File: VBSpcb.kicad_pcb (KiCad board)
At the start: 2 copper layers, 38 x 31.5 mm, 14 parts, among them J1 Conn_01x03, J2 DB25_Receptacle, U1 LF356

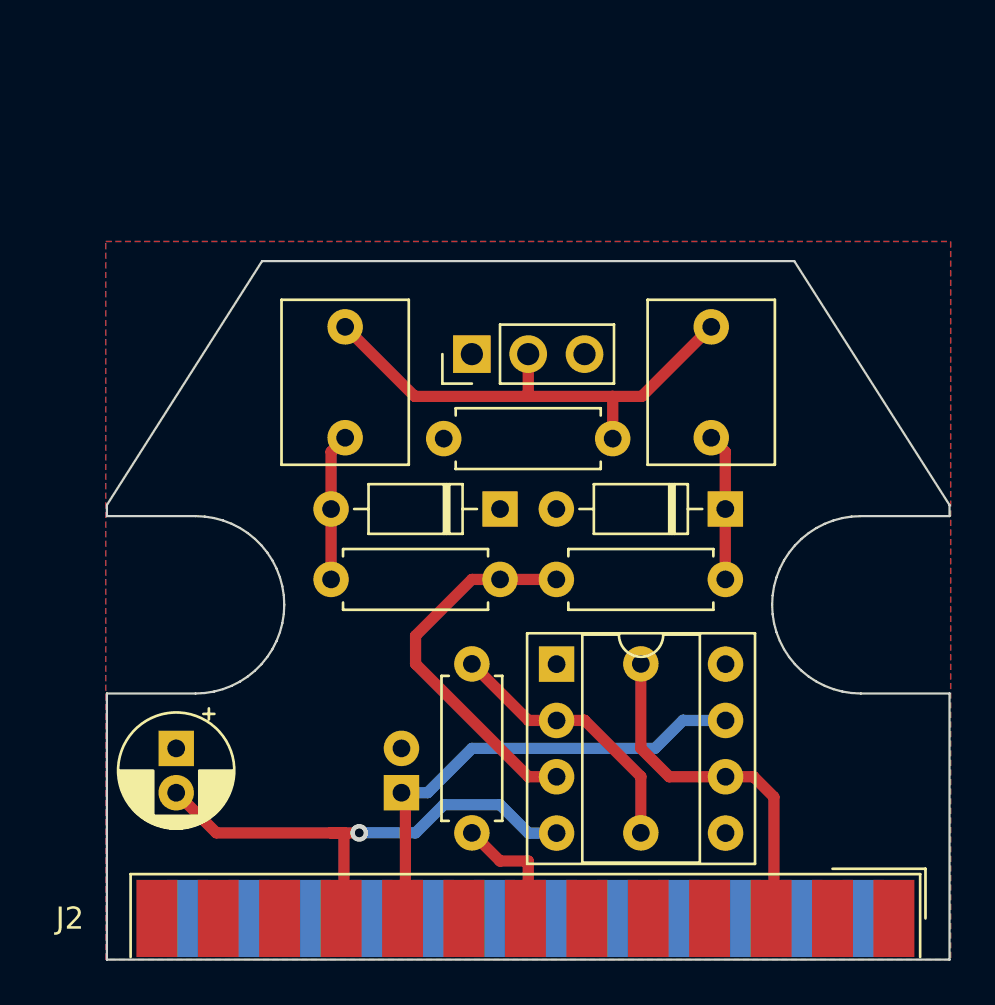
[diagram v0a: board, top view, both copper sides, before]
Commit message: Updated Silkscreen
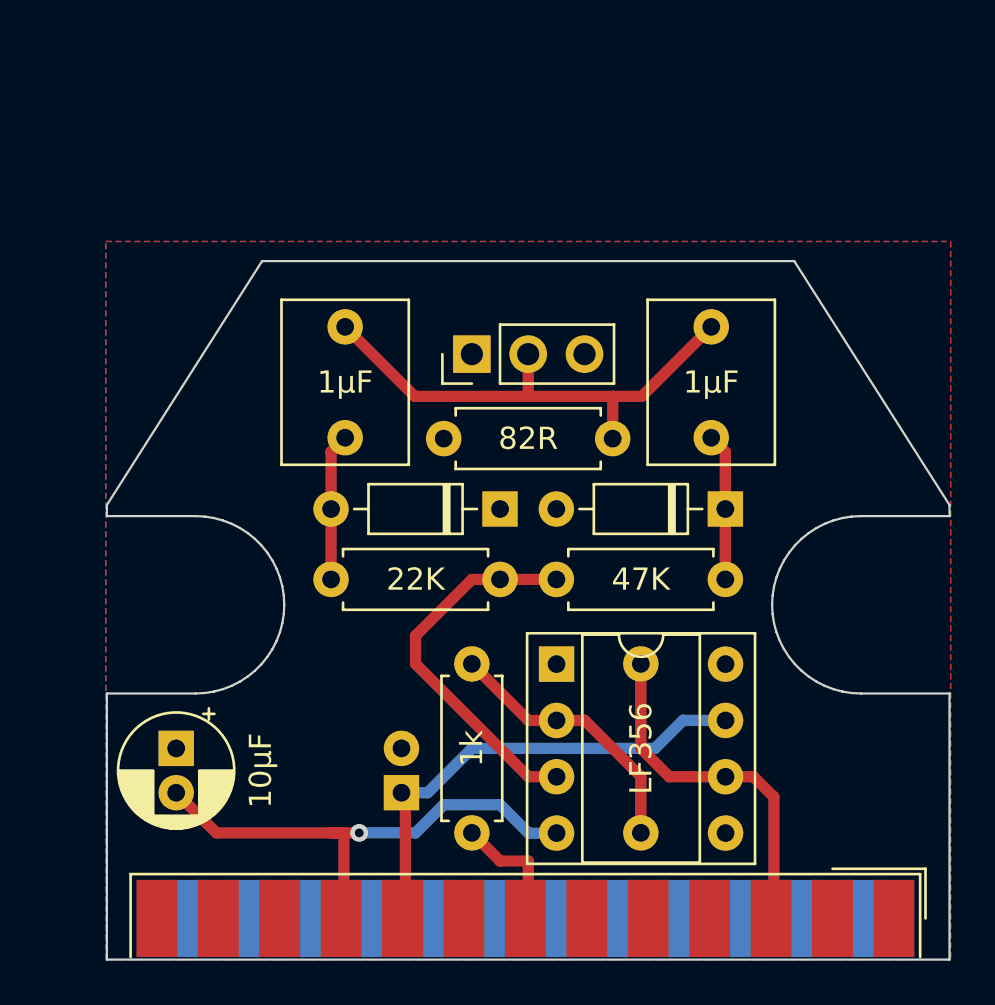
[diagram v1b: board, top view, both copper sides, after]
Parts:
- J1: value Conn_01x03 -> Video In
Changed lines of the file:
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@@
         (effects (font (size 1 1) (thickness 0.15)))
     )
-    (fp_text value "1µF" (at 2.5 0) (layer "F.Fab")
+    (fp_text value "1µF" (at 2.5 0) (layer "F.SilkS")
         (effects (font (size 1 1) (thickness 0.15)))
     )
@@
     (property "ki_keywords" "female receptacle D-SUB connector")
     (attr smd)
-    (fp_text reference "J2" (at -20.543333 0) (layer "F.SilkS")
-        (effects (font (size 1 1) (thickness 0.15)))
-    )
-    (fp_text value "DB25_Receptacle" (at 0 16.86) (layer "F.Fab")
-        (effects (font (size 1 1) (thickness 0.15)))
-    )
-    (fp_text user "PCB edge" (at -21.55 1.323333) (layer "Dwgs.User")
+    (fp_text reference "J2" (at -20.543333 0) (layer "F.SilkS") hide
+        (effects (font (size 1 1) (thickness 0.15)))
+    )
+    (fp_text value "DB25_Receptacle" (at 0 16.86) (layer "F.SilkS") hide
+        (effects (font (size 1 1) (thickness 0.15)))
+    )
+    (fp_text user "PCB edge" (at -21.55 1.323333) (layer "Dwgs.User") hide
         (effects (font (size 0.5 0.5) (thickness 0.075)))
     )
-    (fp_text user "${REFERENCE}" (at 0 3.39) (layer "F.Fab")
+    (fp_text user "${REFERENCE}" (at 0 3.39) (layer "F.Fab") hide
         (effects (font (size 1 1) (thickness 0.15)))
     )
@@
         (effects (font (size 1 1) (thickness 0.15)))
     )
-    (fp_text value "1N4148" (at 3.81 2.12) (layer "F.Fab") hide
+    (fp_text value "1N4148" (at 3.81 2.12) (layer "F.SilkS") hide
         (effects (font (size 1 1) (thickness 0.15)))
     )
@@
         (effects (font (size 1 1) (thickness 0.15)))
     )
-    (fp_text value "1k" (at 3.81 0 -270) (layer "F.Fab")
+    (fp_text value "1k" (at 3.81 0 -270) (layer "F.SilkS")
         (effects (font (size 1 1) (thickness 0.15)))
     )
@@
         (effects (font (size 1 1) (thickness 0.15)))
     )
-    (fp_text value "10µF" (at 1 -3.81 -270) (layer "F.Fab")
+    (fp_text value "10µF" (at 1 -3.81 -270) (layer "F.SilkS")
         (effects (font (size 1 1) (thickness 0.15)))
     )
@@
         (effects (font (size 1 1) (thickness 0.15)))
     )
-    (fp_text value "47K" (at 3.81 0) (layer "F.Fab")
+    (fp_text value "47K" (at 3.81 0) (layer "F.SilkS")
         (effects (font (size 1 1) (thickness 0.15)))
     )
@@
         (effects (font (size 1 1) (thickness 0.15)))
     )
-    (fp_text value "1N4148" (at 3.81 2.12) (layer "F.Fab") hide
+    (fp_text value "1N4148" (at 3.81 2.12) (layer "F.SilkS") hide
         (effects (font (size 1 1) (thickness 0.15)))
     )
@@
         (effects (font (size 1 1) (thickness 0.15)))
     )
-    (fp_text value "22K" (at 3.81 0) (layer "F.Fab")
+    (fp_text value "22K" (at 3.81 0) (layer "F.SilkS")
         (effects (font (size 1 1) (thickness 0.15)))
     )
@@
         (effects (font (size 1 1) (thickness 0.15)))
     )
-    (fp_text value "1µF" (at 2.5 0) (layer "F.Fab")
+    (fp_text value "1µF" (at 2.5 0) (layer "F.SilkS")
         (effects (font (size 1 1) (thickness 0.15)))
     )
@@
         (effects (font (size 1 1) (thickness 0.15)))
     )
-    (fp_text value "82R" (at 3.81 0) (layer "F.Fab")
+    (fp_text value "82R" (at 3.81 0) (layer "F.SilkS")
         (effects (font (size 1 1) (thickness 0.15)))
     )
@@
         (effects (font (size 1 1) (thickness 0.15)))
     )
-    (fp_text value "LF356" (at 3.81 3.8 90) (layer "F.Fab")
+    (fp_text value "LF356" (at 3.81 3.8 90) (layer "F.SilkS")
         (effects (font (size 1 1) (thickness 0.15)))
     )
@@
         (effects (font (size 1 1) (thickness 0.15)))
     )
-    (fp_text value "Conn_01x03" (at 0 7.41 90) (layer "F.Fab") hide
+    (fp_text value "Video In" (at 0 7.41 90) (layer "F.SilkS") hide
         (effects (font (size 1 1) (thickness 0.15)))
     )
@@
         (effects (font (size 1 1) (thickness 0.15)) (justify mirror))
     )
-    (fp_text value "9k1" (at 3.81 0 90) (layer "B.Fab")
+    (fp_text value "9k1" (at 3.81 0 90) (layer "B.SilkS")
         (effects (font (size 1 1) (thickness 0.15)) (justify mirror))
     )
@@
         (effects (font (size 1 1) (thickness 0.15)) (justify mirror))
     )
-    (fp_text value "10µF" (at 1 -3.75 90) (layer "B.Fab")
+    (fp_text value "10µF" (at 1 -3.75 90) (layer "B.SilkS")
         (effects (font (size 1 1) (thickness 0.15)) (justify mirror))
     )

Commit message: Added nubbin for strain releif
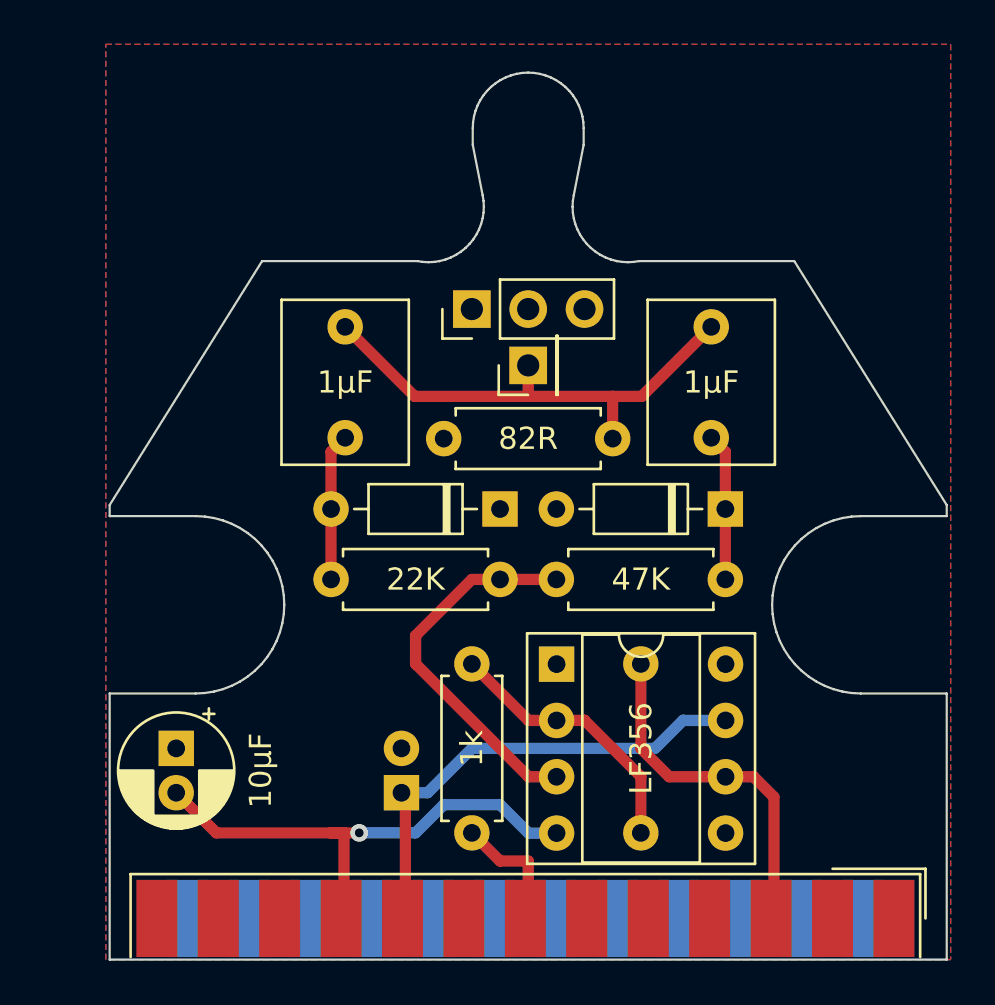
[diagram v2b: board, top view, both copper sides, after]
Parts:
- added J3: Video In Sig, Connector_PinHeader_2.54mm:PinHeader_1x01_P2.54mm_Vertical, F.Cu at (116.8, 67.8)
- J1: value Video In -> Video In GND
- moved J1 2.03 mm to (114.3, 65.3)
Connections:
- C1 pad 1: Net-(J1-Pin_2) -> Net-(J3-Pin_1)
- C2 pad 1: Net-(J1-Pin_2) -> Net-(J3-Pin_1)
- J1 pad 2: Net-(J1-Pin_2) -> GND
- R1 pad 1: Net-(J1-Pin_2) -> Net-(J3-Pin_1)
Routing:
- net Net-(J1-Pin_2): track 22.9 -> 0.00 mm
- net Net-(J3-Pin_1): track 0.00 -> 22.4 mm
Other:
- board size 38 x 31.5 mm -> 37.8 x 40 mm
